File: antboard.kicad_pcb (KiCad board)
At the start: 2 copper layers, 1 part, among them U4 OLED_0.96

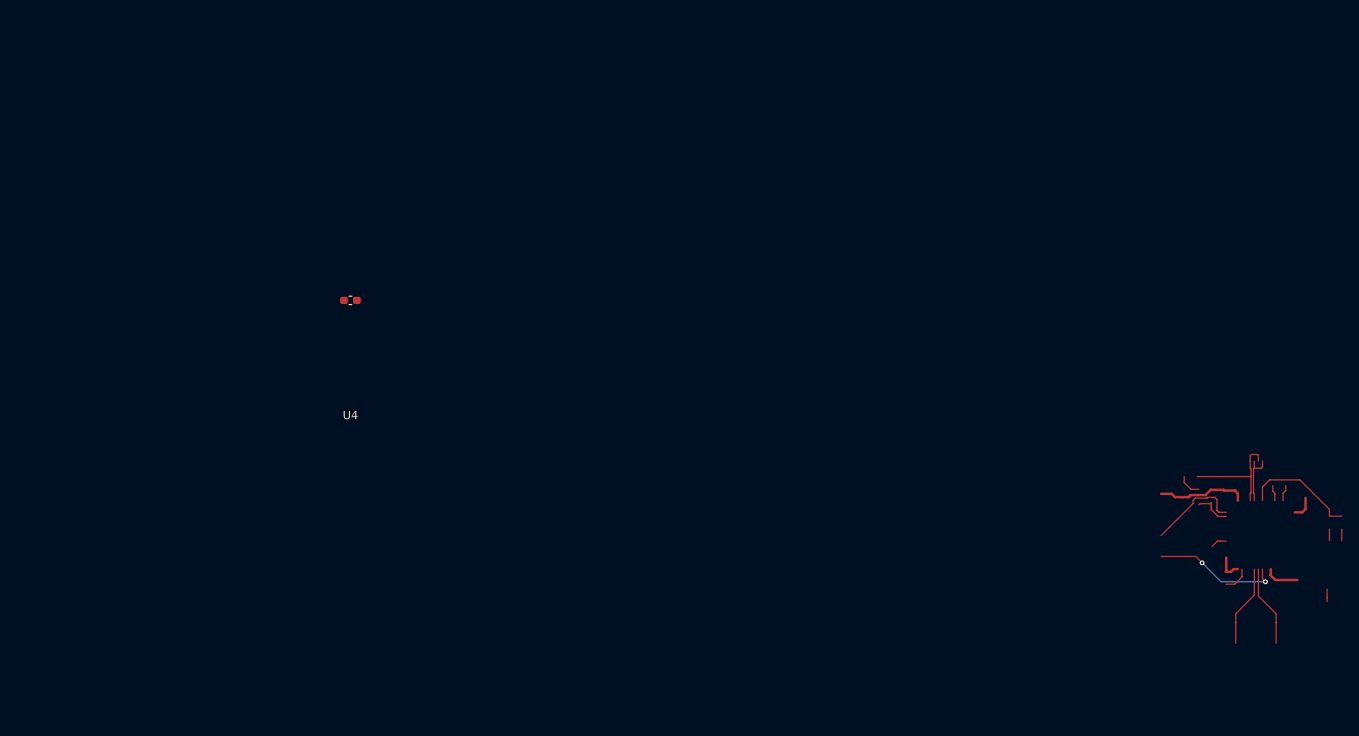
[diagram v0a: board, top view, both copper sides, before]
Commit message: Misc sch fixes and psu p&r done
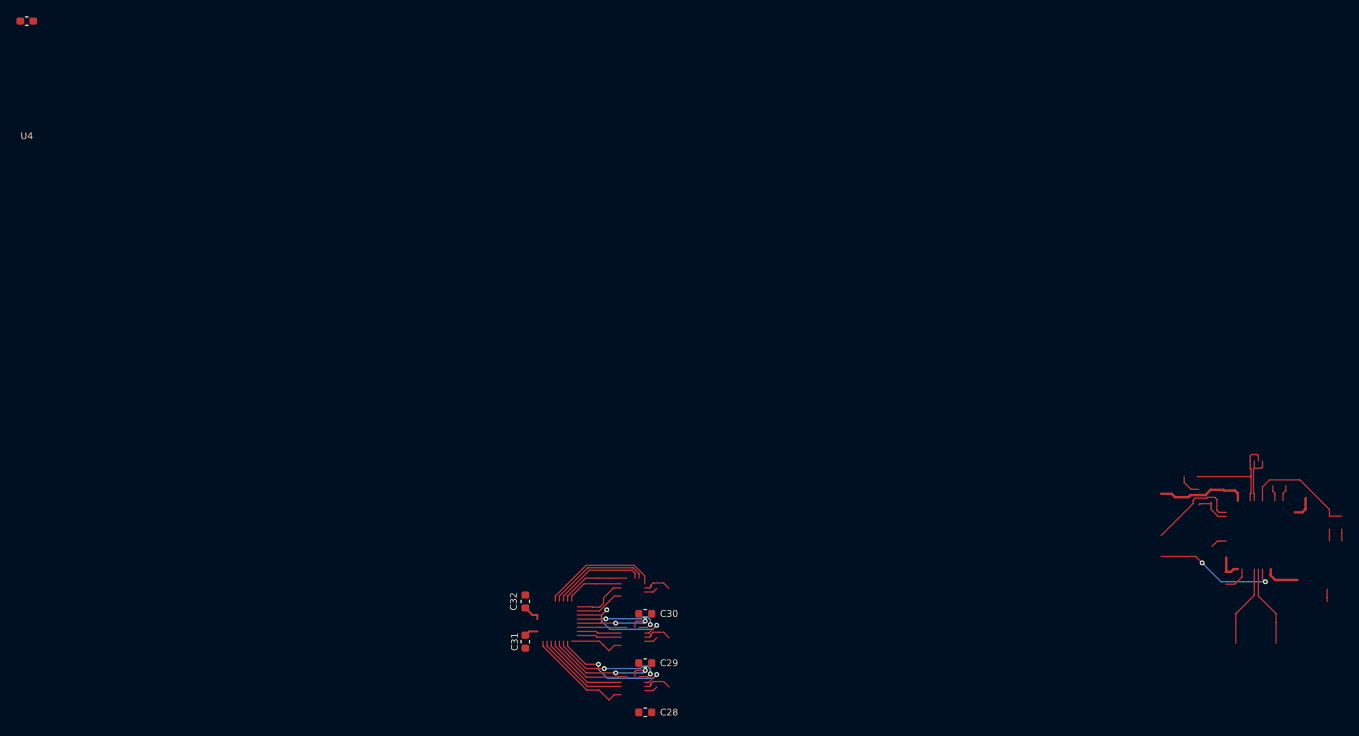
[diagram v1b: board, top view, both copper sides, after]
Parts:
- added C28: 10u, Capacitor_SMD:C_0603_1608Metric, F.Cu at (145.1, 134.6)
- added C29: 10u, Capacitor_SMD:C_0603_1608Metric, F.Cu at (145.1, 128.6)
- added C30: 10u, Capacitor_SMD:C_0603_1608Metric, F.Cu at (145.1, 122.6)
- added C31: 100n, Capacitor_SMD:C_0603_1608Metric, F.Cu at (130.5, 126.0)
- added C32: 100n, Capacitor_SMD:C_0603_1608Metric, F.Cu at (130.5, 121.1)
- moved U4 52.0 mm to (69.8, 50.4)
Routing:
- net /io_power/PAV5: track 0.00 -> 15.5 mm, vias 0 -> 2
- net /io_power/PBV5: track 0.00 -> 14.7 mm, vias 0 -> 2
- net /io_power/PAV10: track 0.00 -> 14.7 mm, vias 0 -> 2
- net /io_power/PCV5: track 0.00 -> 14.5 mm
- net /io_power/PAV20: track 0.00 -> 14.5 mm, vias 0 -> 2
- net /io_power/PAVEN: track 0.00 -> 13.1 mm
- net /io_power/PCV10: track 0.00 -> 12.6 mm
- net /io_power/PAV160: track 0.00 -> 11.7 mm
- net /io_power/PCV20: track 0.00 -> 11.4 mm
- net /io_power/PBV10: track 0.00 -> 11.2 mm, vias 0 -> 2
- net /io_power/PAV80: track 0.00 -> 10.9 mm
- net /io_power/PAV40: track 0.00 -> 10.9 mm
- net /io_power/PBV20: track 0.00 -> 10.3 mm, vias 0 -> 2
- net /io_power/PCV40: track 0.00 -> 8.72 mm
- net /io_power/PCV80: track 0.00 -> 7.25 mm
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
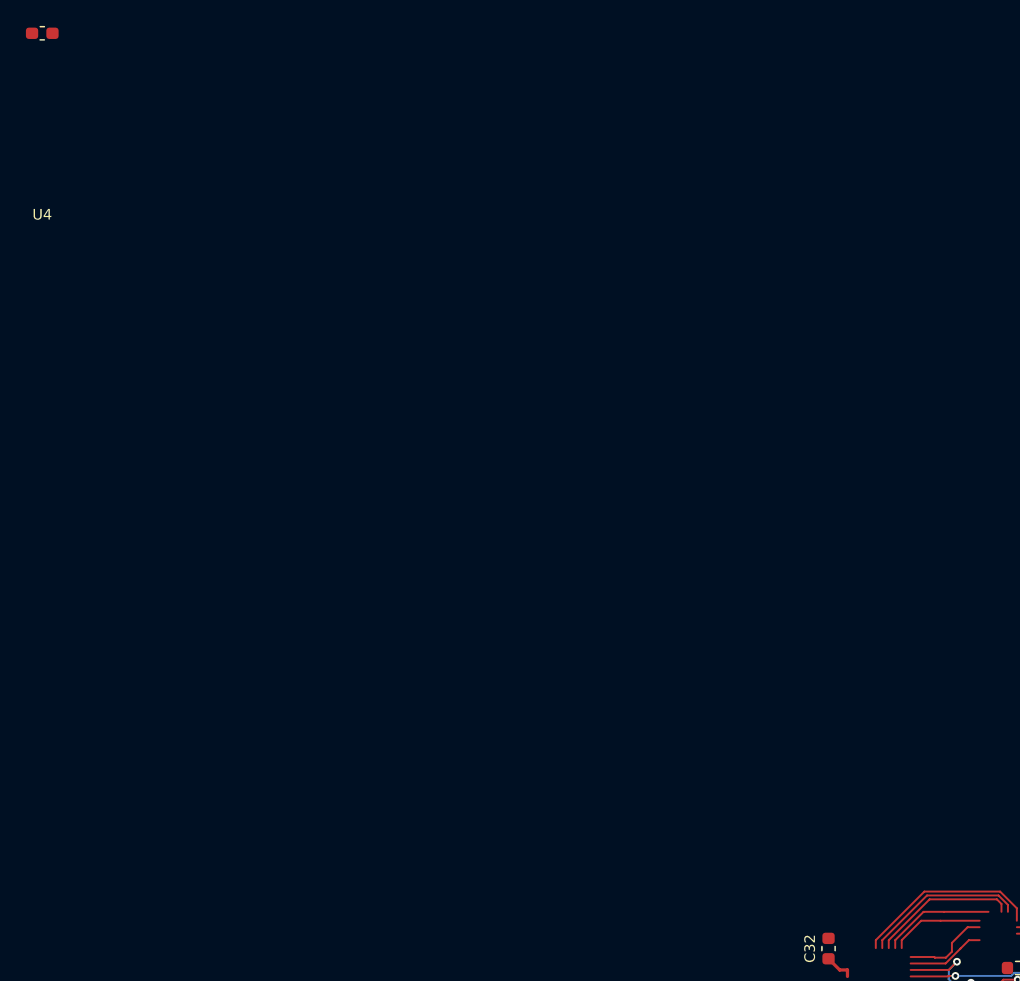
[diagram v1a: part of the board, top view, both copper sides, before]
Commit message: pcb: Place some caps
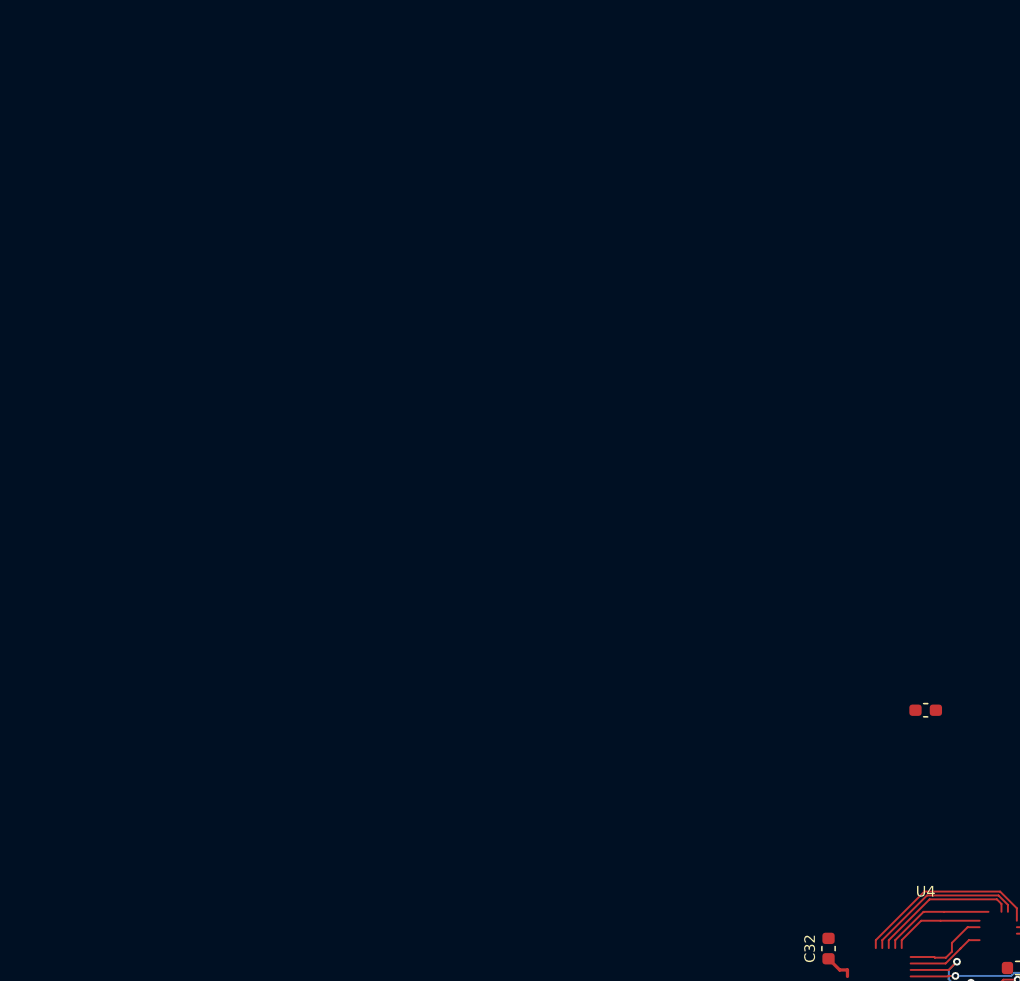
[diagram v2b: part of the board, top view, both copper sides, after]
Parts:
- moved U4 85.9 mm to (138.0, 102.7)
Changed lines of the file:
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@@
   )
   (module antboard:OLED_0.96_SSD1306 (layer F.Cu)
-    (at 69.805 50.445)
+    (at 138 102.7)
     (fp_text reference U4 (at 0 14) (layer F.SilkS)
       (effects (font (size 0.82 0.82) (thickness 0.15)))
@@
   )
   (module Package_QFP:LQFP-64_10x10mm_P0.5mm (layer F.Cu)
-    (at 137.6 104.5 90)
+    (at 101.9 99.2 90)
     (descr "LQFP, 64 Pin (https://www.analog.com/media/en/technical-documentation/data-sheets/ad7606_7606-6_7606-4.pdf), generated with kicad-footprint-generator ipc_gullwing_generator.py")
     (tags "LQFP QFP")
@@
   )
   (module Capacitor_SMD:C_0603_1608Metric (layer F.Cu)
-    (at 110.835 39.135)
+    (at 95.1 104.1)
     (descr "Capacitor SMD 0603 (1608 Metric), square (rectangular) end terminal, IPC_7351 nominal, (Body size source: http://www.tortai-tech.com/upload/download/2011102023233369053.pdf), generated with kicad-footprint-generator")
     (tags capacitor)
@@
   )
   (module Capacitor_SMD:C_0603_1608Metric (layer F.Cu)
-    (at 64.255 66.775)
+    (at 95.9 93.5 270)
     (descr "Capacitor SMD 0603 (1608 Metric), square (rectangular) end terminal, IPC_7351 nominal, (Body size source: http://www.tortai-tech.com/upload/download/2011102023233369053.pdf), generated with kicad-footprint-generator")
     (tags capacitor)
     (attr smd)
-    (fp_text reference C16 (at 0 -1.43) (layer F.SilkS)
+    (fp_text reference C16 (at 0 1.4 90) (layer F.SilkS)
       (effects (font (size 0.82 0.82) (thickness 0.15)))
     )
-    (fp_text value 100n (at 0 1.43) (layer F.Fab)
+    (fp_text value 100n (at 0 1.43 90) (layer F.Fab)
       (effects (font (size 0.82 0.82) (thickness 0.15)))
     )
-    (fp_text user %R (at 0 0) (layer F.Fab)
+    (fp_text user %R (at 0 0 90) (layer F.Fab)
       (effects (font (size 0.4 0.4) (thickness 0.06)))
     )
@@
     (fp_line (start -0.8 -0.4) (end 0.8 -0.4) (layer F.Fab) (width 0.1))
     (fp_line (start -0.8 0.4) (end -0.8 -0.4) (layer F.Fab) (width 0.1))
-    (pad 2 smd roundrect (at 0.7875 0) (size 0.875 0.95) (layers F.Cu F.Paste F.Mask) (roundrect_rratio 0.25)
+    (pad 2 smd roundrect (at 0.7875 0 270) (size 0.875 0.95) (layers F.Cu F.Paste F.Mask) (roundrect_rratio 0.25)
       (net 1 GND))
-    (pad 1 smd roundrect (at -0.7875 0) (size 0.875 0.95) (layers F.Cu F.Paste F.Mask) (roundrect_rratio 0.25)
+    (pad 1 smd roundrect (at -0.7875 0 270) (size 0.875 0.95) (layers F.Cu F.Paste F.Mask) (roundrect_rratio 0.25)
       (net 2 +3V3))
     (model ${KISYS3DMOD}/Capacitor_SMD.3dshapes/C_0603_1608Metric.wrl
@@
   )
   (module Capacitor_SMD:C_0603_1608Metric (layer F.Cu)
-    (at 60.245 66.775)
+    (at 107.6 93.2 180)
     (descr "Capacitor SMD 0603 (1608 Metric), square (rectangular) end terminal, IPC_7351 nominal, (Body size source: http://www.tortai-tech.com/upload/download/2011102023233369053.pdf), generated with kicad-footprint-generator")
     (tags capacitor)
     (attr smd)
-    (fp_text reference C15 (at 0 -1.43) (layer F.SilkS)
+    (fp_text reference C15 (at 0 1.3) (layer F.SilkS)
       (effects (font (size 0.82 0.82) (thickness 0.15)))
     )
@@
     (fp_line (start -0.8 -0.4) (end 0.8 -0.4) (layer F.Fab) (width 0.1))
     (fp_line (start -0.8 0.4) (end -0.8 -0.4) (layer F.Fab) (width 0.1))
-    (pad 2 smd roundrect (at 0.7875 0) (size 0.875 0.95) (layers F.Cu F.Paste F.Mask) (roundrect_rratio 0.25)
+    (pad 2 smd roundrect (at 0.7875 0 180) (size 0.875 0.95) (layers F.Cu F.Paste F.Mask) (roundrect_rratio 0.25)
       (net 1 GND))
-    (pad 1 smd roundrect (at -0.7875 0) (size 0.875 0.95) (layers F.Cu F.Paste F.Mask) (roundrect_rratio 0.25)
+    (pad 1 smd roundrect (at -0.7875 0 180) (size 0.875 0.95) (layers F.Cu F.Paste F.Mask) (roundrect_rratio 0.25)
       (net 2 +3V3))
     (model ${KISYS3DMOD}/Capacitor_SMD.3dshapes/C_0603_1608Metric.wrl
@@
   )
   (module Capacitor_SMD:C_0603_1608Metric (layer F.Cu)
-    (at 56.235 66.775)
+    (at 111.7 102.1)
     (descr "Capacitor SMD 0603 (1608 Metric), square (rectangular) end terminal, IPC_7351 nominal, (Body size source: http://www.tortai-tech.com/upload/download/2011102023233369053.pdf), generated with kicad-footprint-generator")
     (tags capacitor)
@@
   )
   (module Capacitor_SMD:C_0603_1608Metric (layer F.Cu)
-    (at 87.385 66.305)
+    (at 104.1 108.7 270)
     (descr "Capacitor SMD 0603 (1608 Metric), square (rectangular) end terminal, IPC_7351 nominal, (Body size source: http://www.tortai-tech.com/upload/download/2011102023233369053.pdf), generated with kicad-footprint-generator")
     (tags capacitor)
     (attr smd)
-    (fp_text reference C13 (at 0 -1.43) (layer F.SilkS)
+    (fp_text reference C13 (at 0 -1.43 90) (layer F.SilkS)
       (effects (font (size 0.82 0.82) (thickness 0.15)))
     )
-    (fp_text value 100n (at 0 1.43) (layer F.Fab)
+    (fp_text value 100n (at 0 1.43 90) (layer F.Fab)
       (effects (font (size 0.82 0.82) (thickness 0.15)))
     )
-    (fp_text user %R (at 0 0) (layer F.Fab)
+    (fp_text user %R (at 0 0 90) (layer F.Fab)
       (effects (font (size 0.4 0.4) (thickness 0.06)))
     )
@@
     (fp_line (start -0.8 -0.4) (end 0.8 -0.4) (layer F.Fab) (width 0.1))
     (fp_line (start -0.8 0.4) (end -0.8 -0.4) (layer F.Fab) (width 0.1))
-    (pad 2 smd roundrect (at 0.7875 0) (size 0.875 0.95) (layers F.Cu F.Paste F.Mask) (roundrect_rratio 0.25)
+    (pad 2 smd roundrect (at 0.7875 0 270) (size 0.875 0.95) (layers F.Cu F.Paste F.Mask) (roundrect_rratio 0.25)
       (net 1 GND))
-    (pad 1 smd roundrect (at -0.7875 0) (size 0.875 0.95) (layers F.Cu F.Paste F.Mask) (roundrect_rratio 0.25)
+    (pad 1 smd roundrect (at -0.7875 0 270) (size 0.875 0.95) (layers F.Cu F.Paste F.Mask) (roundrect_rratio 0.25)
       (net 2 +3V3))
     (model ${KISYS3DMOD}/Capacitor_SMD.3dshapes/C_0603_1608Metric.wrl
@@
   )
   (module Capacitor_SMD:C_0603_1608Metric (layer F.Cu)
-    (at 98.975 51.075)
+    (at 96.9 106 90)
     (descr "Capacitor SMD 0603 (1608 Metric), square (rectangular) end terminal, IPC_7351 nominal, (Body size source: http://www.tortai-tech.com/upload/download/2011102023233369053.pdf), generated with kicad-footprint-generator")
     (tags capacitor)
     (attr smd)
-    (fp_text reference C12 (at 0 -1.43) (layer F.SilkS)
+    (fp_text reference C12 (at 0 -1.43 90) (layer F.SilkS)
       (effects (font (size 0.82 0.82) (thickness 0.15)))
     )
-    (fp_text value 100n (at 0 1.43) (layer F.Fab)
+    (fp_text value 100n (at 0 1.43 90) (layer F.Fab)
       (effects (font (size 0.82 0.82) (thickness 0.15)))
     )
-    (fp_text user %R (at 0 0) (layer F.Fab)
+    (fp_text user %R (at 0 0 90) (layer F.Fab)
       (effects (font (size 0.4 0.4) (thickness 0.06)))
     )
@@
     (fp_line (start -0.8 -0.4) (end 0.8 -0.4) (layer F.Fab) (width 0.1))
     (fp_line (start -0.8 0.4) (end -0.8 -0.4) (layer F.Fab) (width 0.1))
-    (pad 2 smd roundrect (at 0.7875 0) (size 0.875 0.95) (layers F.Cu F.Paste F.Mask) (roundrect_rratio 0.25)
+    (pad 2 smd roundrect (at 0.7875 0 90) (size 0.875 0.95) (layers F.Cu F.Paste F.Mask) (roundrect_rratio 0.25)
       (net 1 GND))
-    (pad 1 smd roundrect (at -0.7875 0) (size 0.875 0.95) (layers F.Cu F.Paste F.Mask) (roundrect_rratio 0.25)
+    (pad 1 smd roundrect (at -0.7875 0 90) (size 0.875 0.95) (layers F.Cu F.Paste F.Mask) (roundrect_rratio 0.25)
       (net 2 +3V3))
     (model ${KISYS3DMOD}/Capacitor_SMD.3dshapes/C_0603_1608Metric.wrl
